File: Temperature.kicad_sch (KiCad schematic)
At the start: 13 parts, among them J3 Conn_01x24_Female, U1 ADS7953SBDBT, U2 REF35160QDBVR, U3 LM321

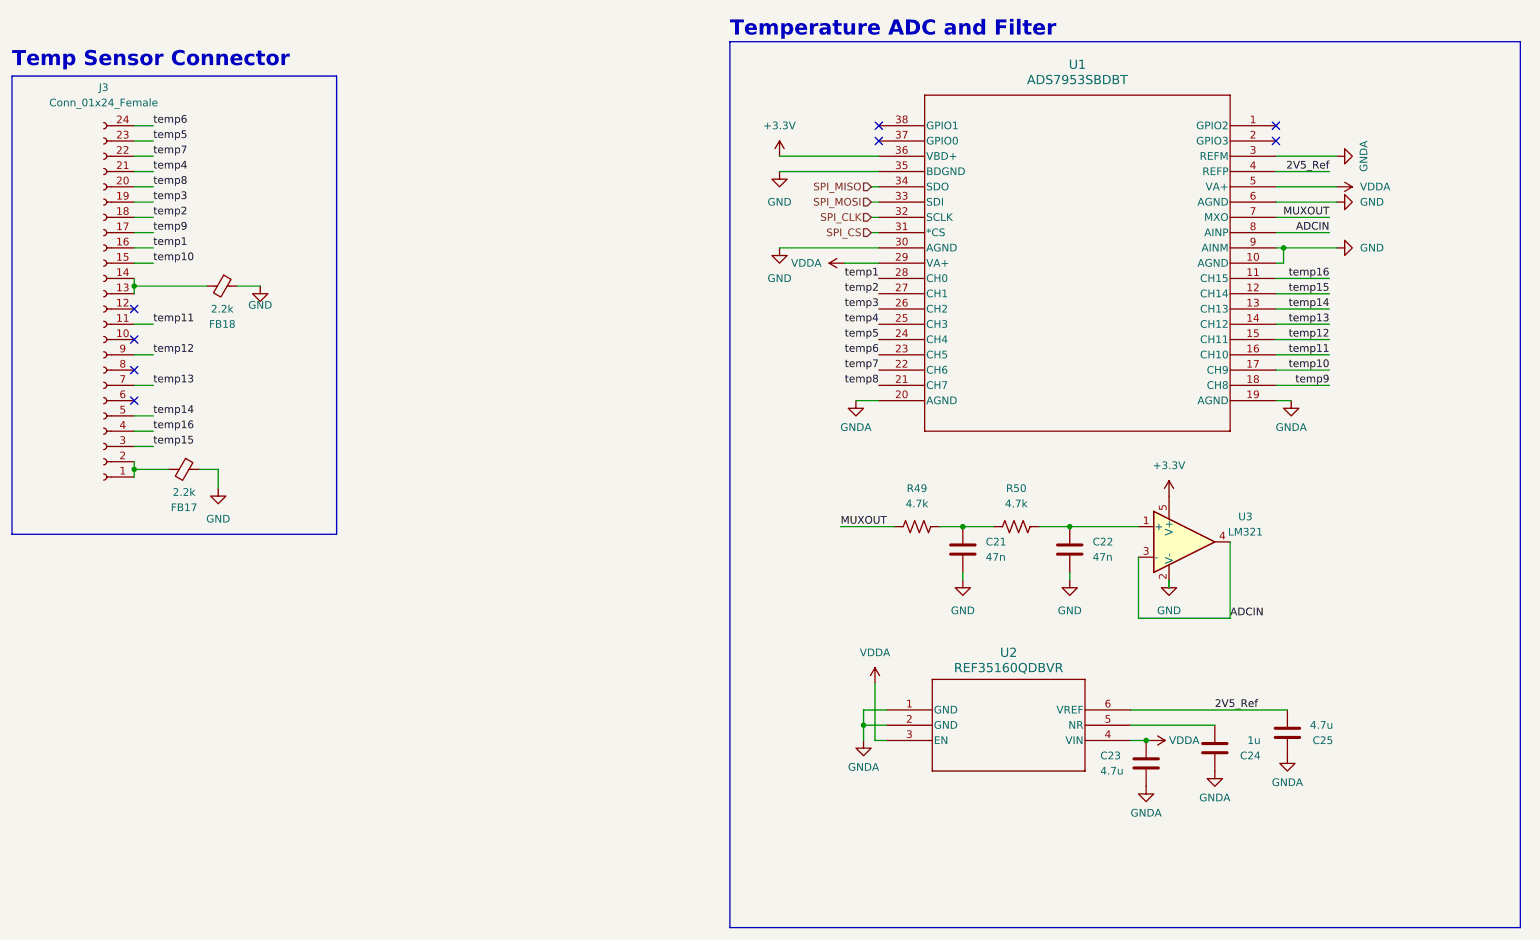
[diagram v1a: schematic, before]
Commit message: temperature fixes
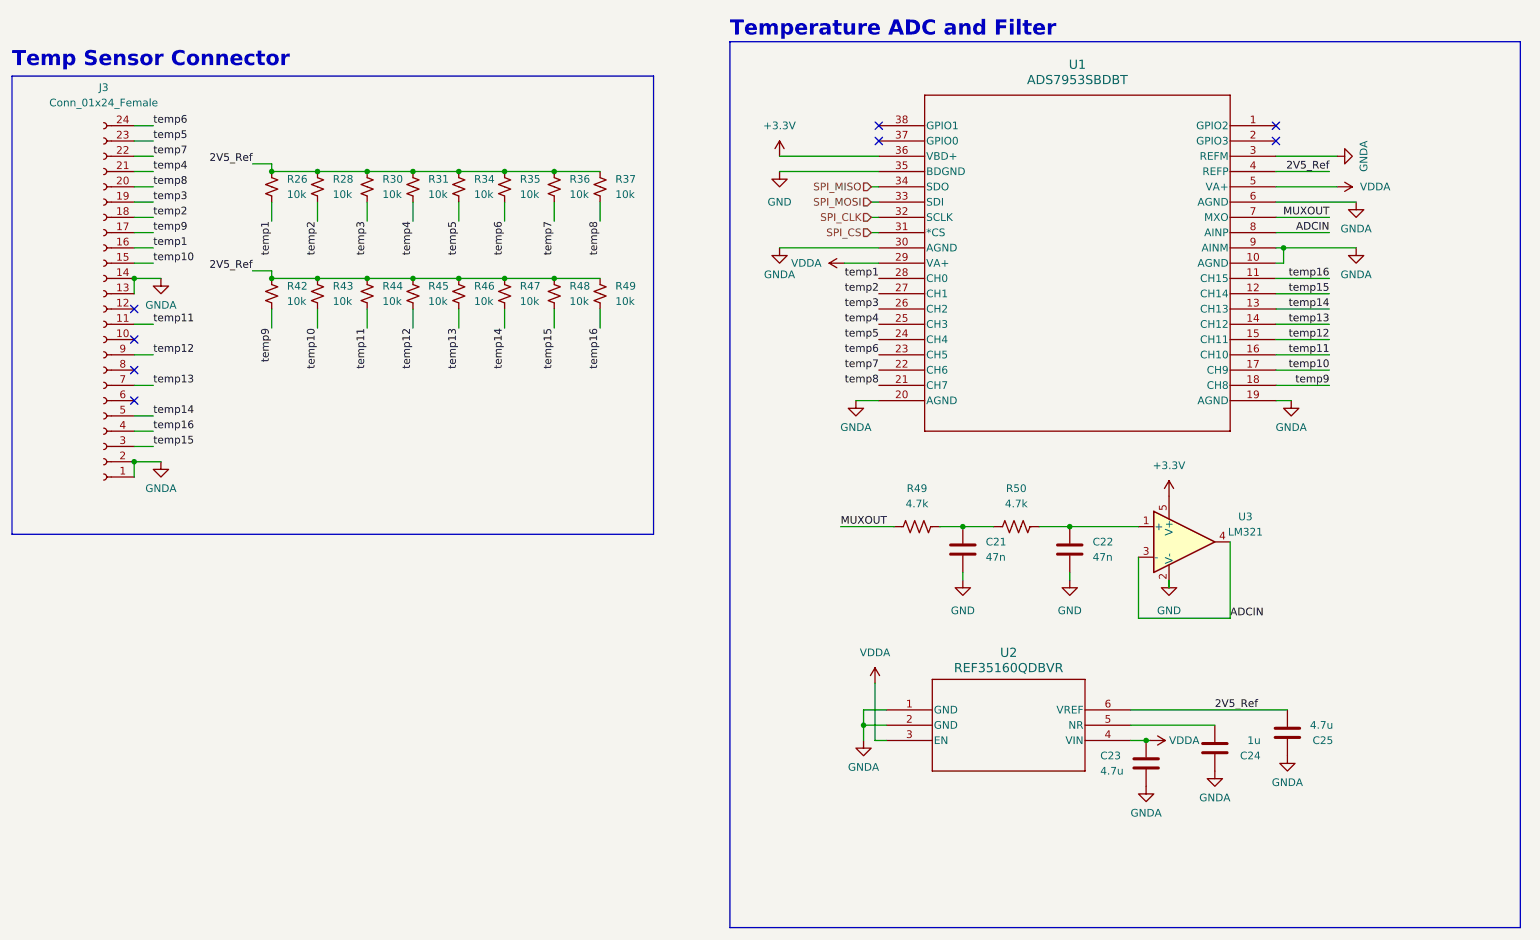
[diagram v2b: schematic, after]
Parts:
- removed FB17, FB18: 2.2k, Inductor_SMD:L_0805_2012Metric_Pad1.05x1.20mm_HandSolder, symbol Device:FerriteBead_Small
- added R26, R28, R30, R31, R34, R35, R36, R37, R42, R43, R44, R45, R46, R47, R48, R49: 10k, Resistor_SMD:R_0805_2012Metric, symbol Device:R_Small_US
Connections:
- net 2V5_Ref: now also R26.2, R28.2, R30.2, R31.2, R34.2, R35.2, R36.2, R37.2, R42.2, R43.2, R44.2, R45.2, R46.2, R47.2, R48.2, R49.2
- net GND: no longer U1.10 (AGND), U1.30 (AGND), U1.6 (AGND), U1.9 (AINM)
- net GNDA: now also J3.1 (Pin_1), J3.13 (Pin_13), J3.14 (Pin_14), J3.2 (Pin_2), U1.10 (AGND), U1.30 (AGND), U1.6 (AGND), U1.9 (AINM)
- net temp1: now also R26.1
- net temp10: now also R43.1
- net temp11: now also R44.1
- net temp12: now also R45.1
- net temp13: now also R46.1
- net temp14: now also R47.1
- net temp15: now also R48.1
- net temp16: now also R49.1
- net temp2: now also R28.1
- net temp3: now also R30.1
- net temp4: now also R31.1
- net temp5: now also R34.1
- net temp6: now also R35.1
- net temp7: now also R36.1
- net temp8: now also R37.1
- net temp9: now also R42.1

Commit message: bypass capacitors
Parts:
- added C24 (x3): 1u, Capacitor_SMD:C_0805_2012Metric_Pad1.18x1.45mm_HandSolder, symbol Device:C
- C25: value 4.7u -> 10u
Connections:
- net +3.3V: now also C24.2
- net GND: now also C24.1
- net GNDA: now also C24.2, C24.2
- net VDDA: now also C24.1, C24.1

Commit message: lakshay changes:
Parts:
- U2: value REF35160QDBVR -> REF35250QDBVR
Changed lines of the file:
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@@
       (effects (font (size 1.524 1.524)))
     )
-    (property "Value" "REF35160QDBVR" (at 193.04 121.92 0)
+    (property "Value" "REF35250QDBVR" (at 193.04 121.92 0)
       (effects (font (size 1.524 1.524)))
     )
@@
       (effects (font (size 1.27 1.27) italic) hide)
     )
-    (property "Datasheet" "REF35160QDBVR" (at 172.72 128.905 0)
+    (property "Datasheet" "REF35250QDBVR" (at 172.72 128.905 0)
       (effects (font (size 1.27 1.27) italic) hide)
     )

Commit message: define edge cuts for new volttemp
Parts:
- U1: footprint Package_SO:HTSSOP-38-1EP_6.1x12.5mm_P0.65mm_EP5.2x12.5mm_Mask3.39x6.35mm -> Package_SO:TSSOP-38_4.4x9.7mm_P0.5mm
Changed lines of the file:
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@@
       (effects (font (size 1.524 1.524)))
     )
-    (property "Footprint" "Package_SO:HTSSOP-38-1EP_6.1x12.5mm_P0.65mm_EP5.2x12.5mm_Mask3.39x6.35mm" (at 237.49 31.75 0)
+    (property "Footprint" "Package_SO:TSSOP-38_4.4x9.7mm_P0.5mm" (at 237.49 31.75 0)
       (effects (font (size 1.27 1.27) italic) hide)
     )

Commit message: why so many bugs >:(
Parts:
- removed C23: 4.7u, Capacitor_SMD:C_0805_2012Metric_Pad1.18x1.45mm_HandSolder, symbol Device:C
- removed C24: 1u, Capacitor_SMD:C_0805_2012Metric_Pad1.18x1.45mm_HandSolder, symbol Device:C
- removed C25: 10u, Capacitor_SMD:C_0805_2012Metric_Pad1.18x1.45mm_HandSolder, symbol Device:C
- removed U2: REF35250QDBVR, Package_SO:TSOP-6_1.65x3.05mm_P0.95mm, symbol utsvt-power-regulators:REF35160QDBVR
- renumbered R26 to R17, R42 to R18, R28 to R19, R43 to R20, R30 to R21, R44 to R22, R31 to R23, R45 to R24, R34 to R25, R46 to R26, R35 to R27, R47 to R28, R36 to R29, R48 to R30, R37 to R31, R49 to R32
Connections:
- net 2V5_Ref renamed +2V5
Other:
- moved on the sheet: R18, R20, R22, R24, R26, R28, R30, R32

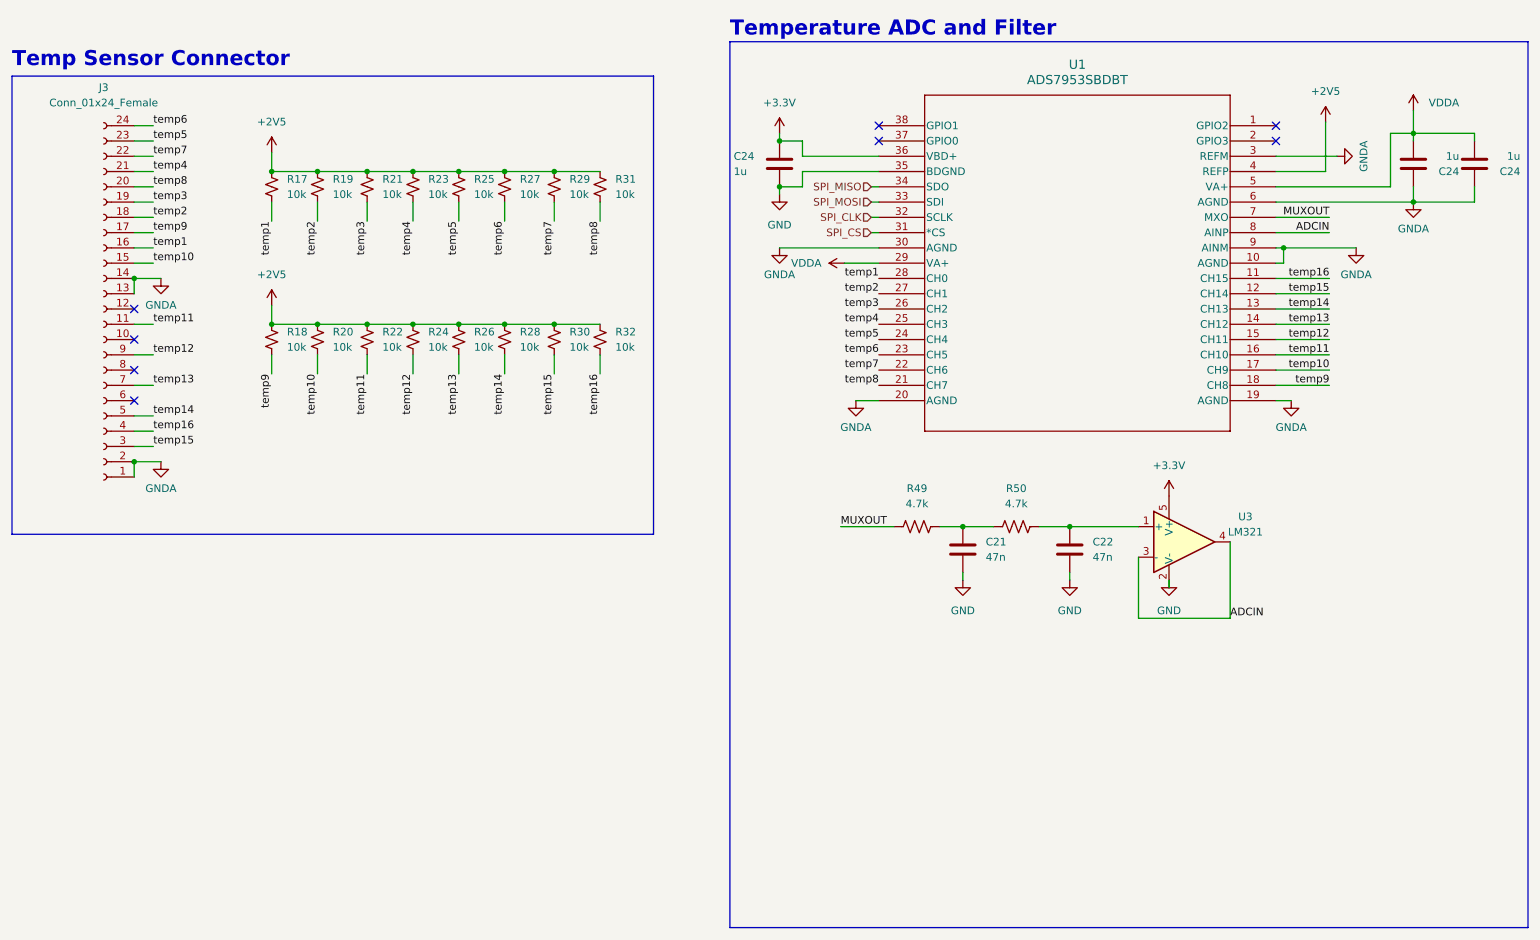
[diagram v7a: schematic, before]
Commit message: Fixed minor bugs with BMS and temp chips
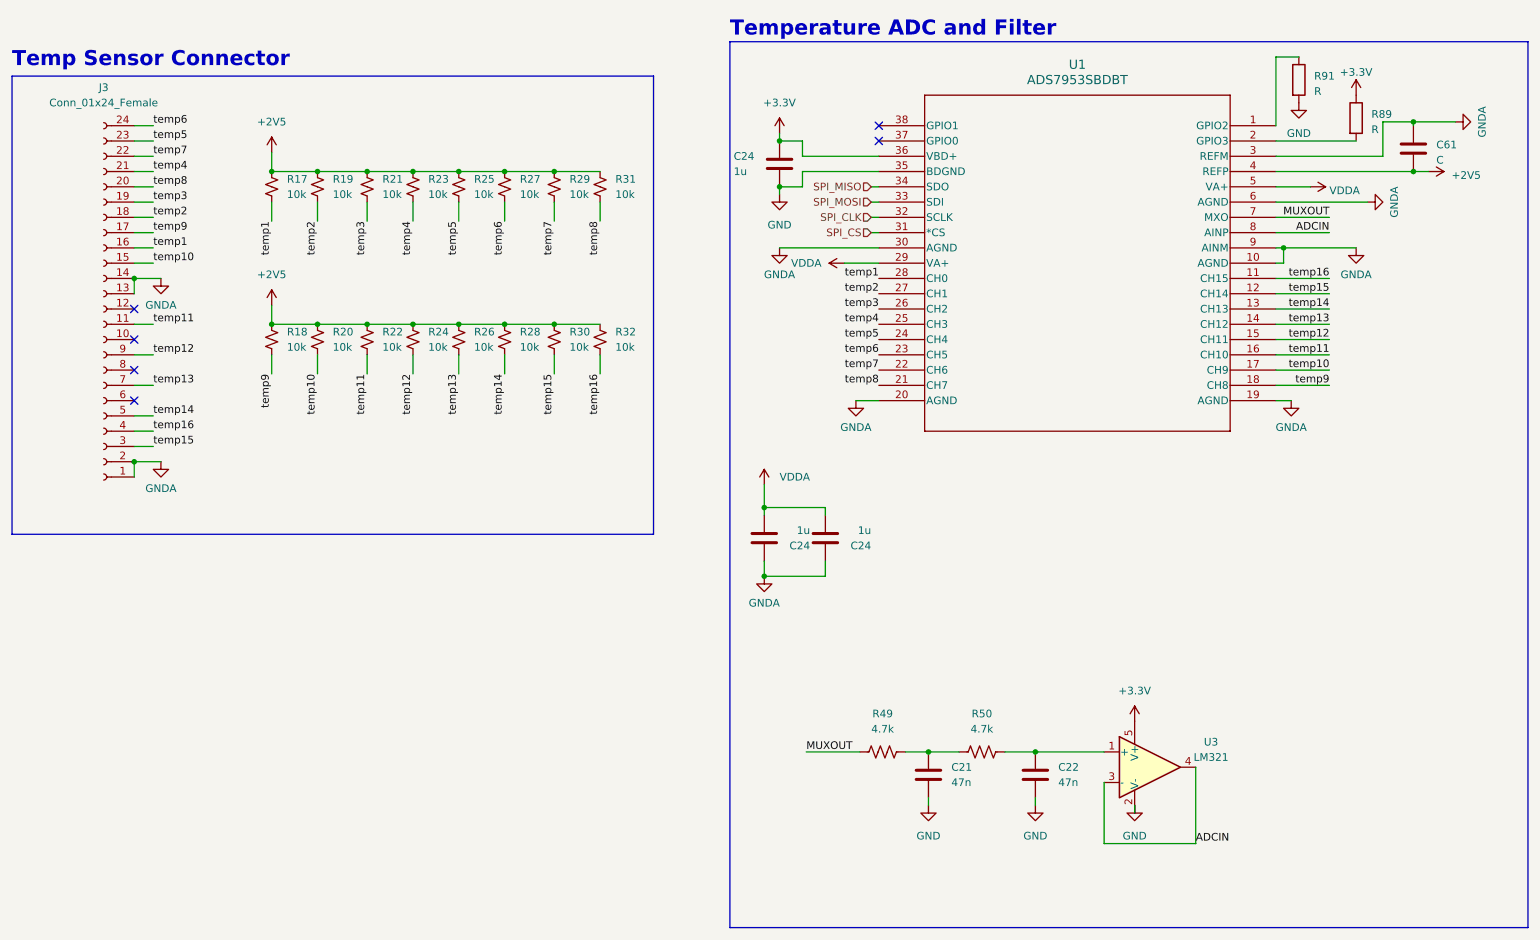
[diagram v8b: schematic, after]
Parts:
- added C61: C, symbol Device:C
- added R89, R91: R, symbol Device:R
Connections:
- net +2V5: now also C61.2
- net +3.3V: now also R89.1
- net GND: now also R91.2
- net GNDA: now also C61.1
- net at U1.1 (GPIO2): now also R91.1
- net at U1.2 (GPIO3): now also R89.2
- no-connect marks 8 -> 6
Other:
- moved on the sheet: C21, C22, C24, R49, R50, U3
